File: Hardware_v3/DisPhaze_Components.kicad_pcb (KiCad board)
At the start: 2 copper layers, 60 x 110 mm, 83 parts, among them J1 SWD_Header, J2 Eurorack_16_pin_power, J3 PD1_Amt_In, J4 DAC1_Out, J5 PItch_In, J6 DAC2_Out, J7 PD2_Amt_In, J8 VCA_In, J9 USB_B_Micro, SW1 Octave_Switch, SW2 DAC1_RingMod_Switch, SW3 DAC2_Mix_Switch, SW4 SW_Push, U1 TL072, U2 MCP6004, U3 LM1117-3.3, U4 STM32F405RGTx, U5 LM4040DBZ-5, Y1 12MHz

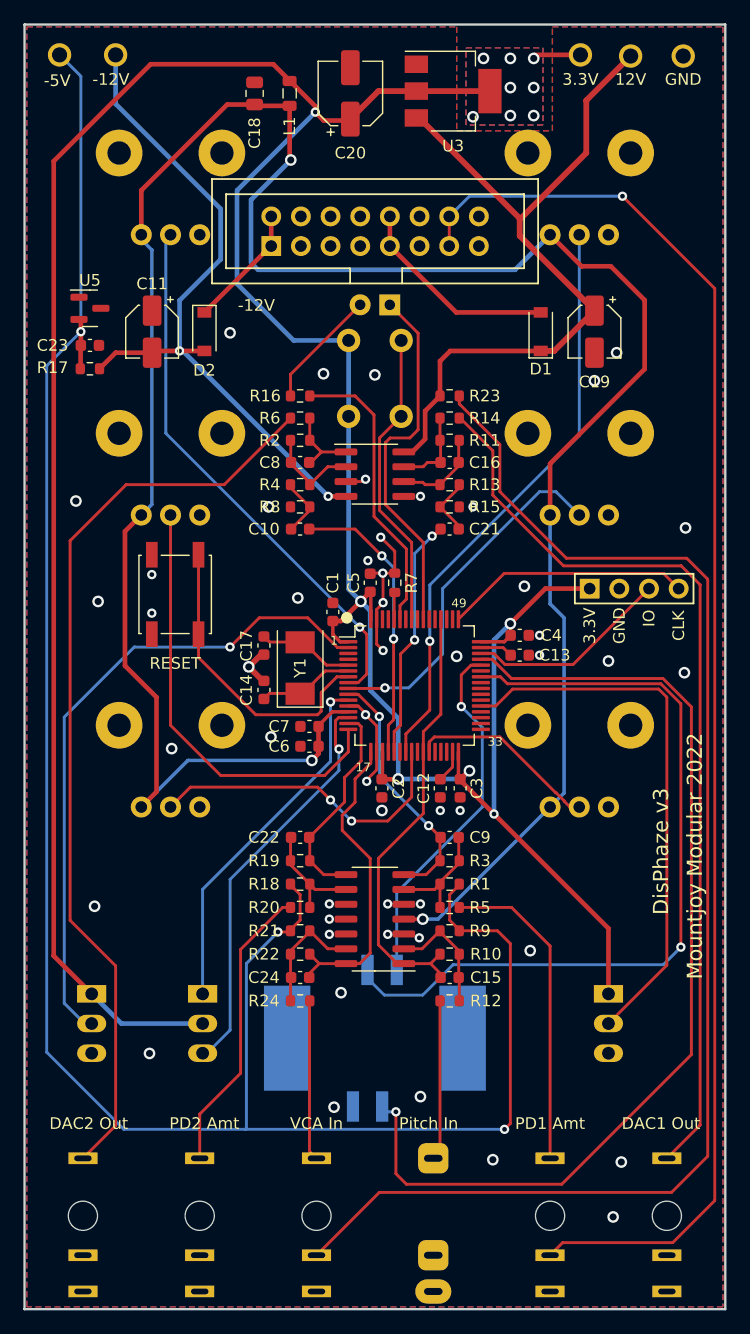
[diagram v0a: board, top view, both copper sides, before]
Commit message: Updated panel to incorporate v3 redesign
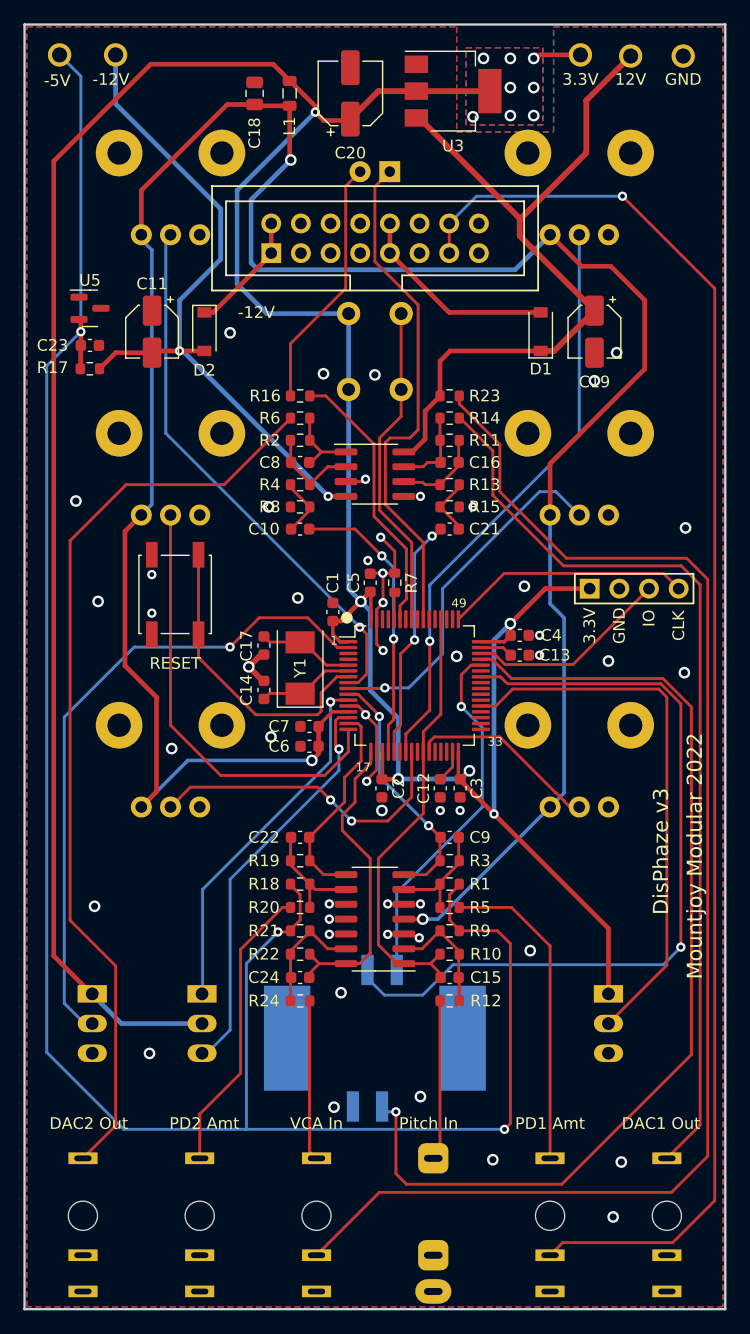
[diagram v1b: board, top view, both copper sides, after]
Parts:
- CTune1, FTune1, PD1Amt1, PD1Type1, PD2Amt1, PD2Type1: footprint Custom_Footprints:Alpha_9mm_Potentiometer -> Custom_Footprints:Alpha_9mm_Potentiometer_Aligned
- moved D3 11.4 mm to (131.3, 62.6)
- moved CTune1 7.91 mm to (147.5, 109.5), turned to 180 degrees
- moved FTune1 7.91 mm to (112.5, 109.5), turned to 180 degrees
- moved PD1Amt1 7.91 mm to (147.5, 60.5), turned to 180 degrees
- moved PD1Type1 7.91 mm to (147.5, 84.5), turned to 180 degrees
- moved PD2Amt1 7.91 mm to (112.5, 60.5), turned to 180 degrees
- moved PD2Type1 7.91 mm to (112.5, 84.5), turned to 180 degrees
- moved SW4 2.30 mm to (130.0, 78.0)
- moved J2 0.61 mm to (121.1, 69.6)
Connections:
- net /Action renamed /ACTION
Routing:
- net /LED_GREEN: track 31.4 -> 43.9 mm
- net Net-(D3-Pad2): track 10.3 -> 21.7 mm
- net /ACTION: track 25.8 -> 28.1 mm
- net /LED_RED: track 25.1 -> 23.6 mm

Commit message: Added photocoupler to MIDI Input
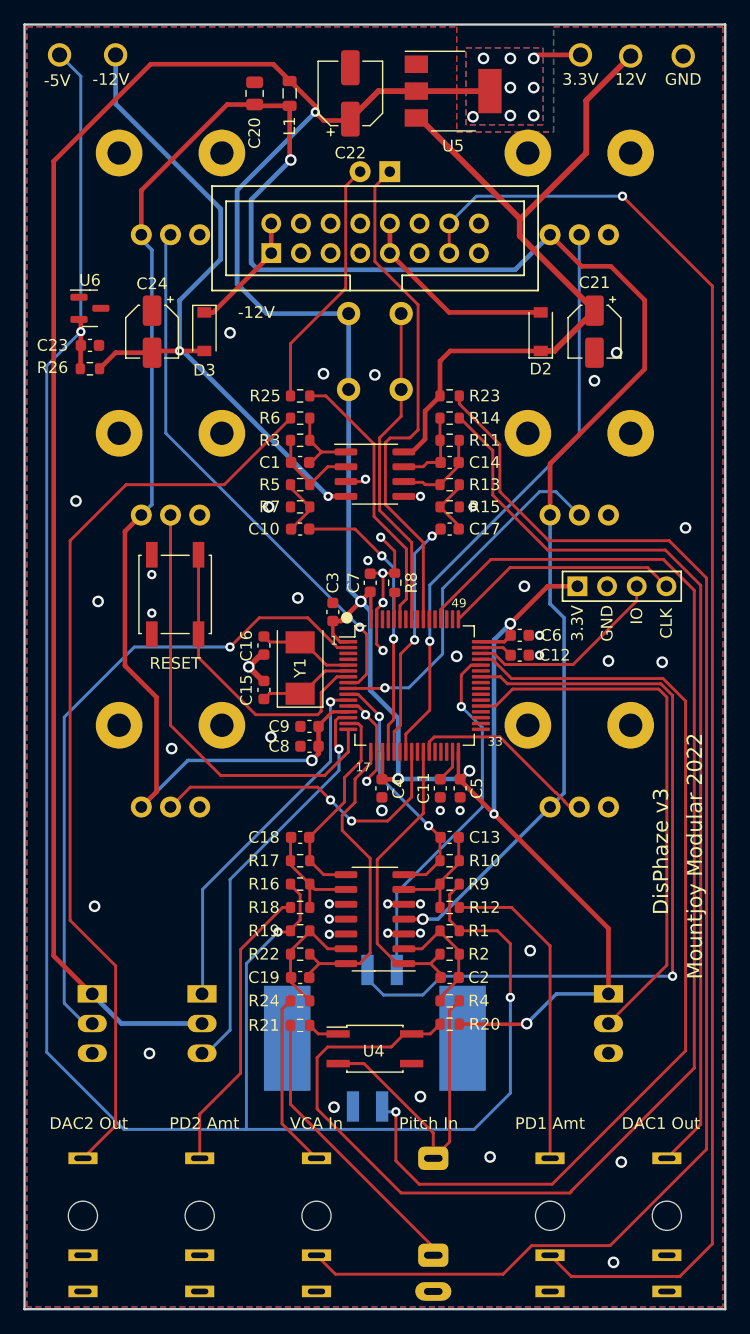
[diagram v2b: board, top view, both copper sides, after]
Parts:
- added R20: 10k, Resistor_SMD:R_0603_1608Metric, F.Cu at (136.4, 135.6)
- added R21: 220, Resistor_SMD:R_0603_1608Metric, F.Cu at (123.6, 135.7)
- added U4: LTV-356T, Package_SO:SO-4_4.4x3.6mm_P2.54mm, F.Cu at (130.0, 137.7)
- moved J6 1.07 mm to (147.3, 98.1)
- turned R24 to 180 degrees
- turned R4 to 0 degrees
- renumbered C8 to C1, C12 to C11, C13 to C12, C9 to C13, C16 to C14, C14 to C15, C17 to C16, C21 to C17, C22 to C18, C24 to C19, C15 to C2, C18 to C20, C19 to C21, C20 to C22, C11 to C24, C1 to C3, C2 to C4, C3 to C5, C4 to C6, C5 to C7, C6 to C8, C7 to C9, D3 to D1, D1 to D2, D2 to D3, J5 to J1, J4 to J2, J6 to J4, J7 to J5, J1 to J6, J9 to J7, J2 to J9, R9 to R1, R3 to R10, R5 to R12, R18 to R16, R19 to R17, R20 to R18, R21 to R19, R10 to R2, R16 to R25, R17 to R26, R2 to R3, R12 to R4, R4 to R5, R8 to R7, R7 to R8, R1 to R9, TP5 to TP1, TP1 to TP2, TP2 to TP3, TP3 to TP4, TP4 to TP5, U2 to U1, U1 to U2, U4 to U3, U3 to U5, U5 to U6
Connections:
- net /Pitch_In renamed /Pitch_MIDI_In
- C2 pad 2: /MIDI_RX -> /V_OCT_CV
- J1 pad R: unconnected-(J5-PadR) -> /MIDI_VREF
- R2 pad 1: /MIDI_RX -> /V_OCT_CV
- U1 pad 1: /MIDI_RX -> /V_OCT_CV
- U3 pad 26: /MIDI_RX -> /V_OCT_CV
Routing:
- net /MIDI_RX: track 37.9 -> 122.2 mm
- net /V_OCT_CV: track 0.00 -> 26.0 mm
- net /MIDI_VREF: track 0.00 -> 24.7 mm
- net /Pitch_MIDI_In: track 13.7 -> 29.4 mm
- net +3V3: track 277.1 -> 289.9 mm, vias 14 -> 15
- net /CV_IN: track 123.0 -> 126.4 mm
- net Net-(R21-Pad1): track 0.00 -> 2.73 mm
- net GND: track 26.4 -> 29.1 mm, vias 50 -> 49
- net /USB_DP: track 86.4 -> 84.9 mm
- net /AREF_-5: track 182.9 -> 181.4 mm
- net /VCA_In: track 13.7 -> 15.0 mm
- net Net-(J8-Pad2): track 117.0 -> 117.8 mm
- net /SWCLK: track 21.0 -> 20.3 mm
- net Net-(C2-Pad1): track 10.5 -> 11.2 mm
- net -12V: track 11.0 -> 10.3 mm
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
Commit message: Replaced optocoupler with transistor pair. Changed bi-colour LED to 3 lead device
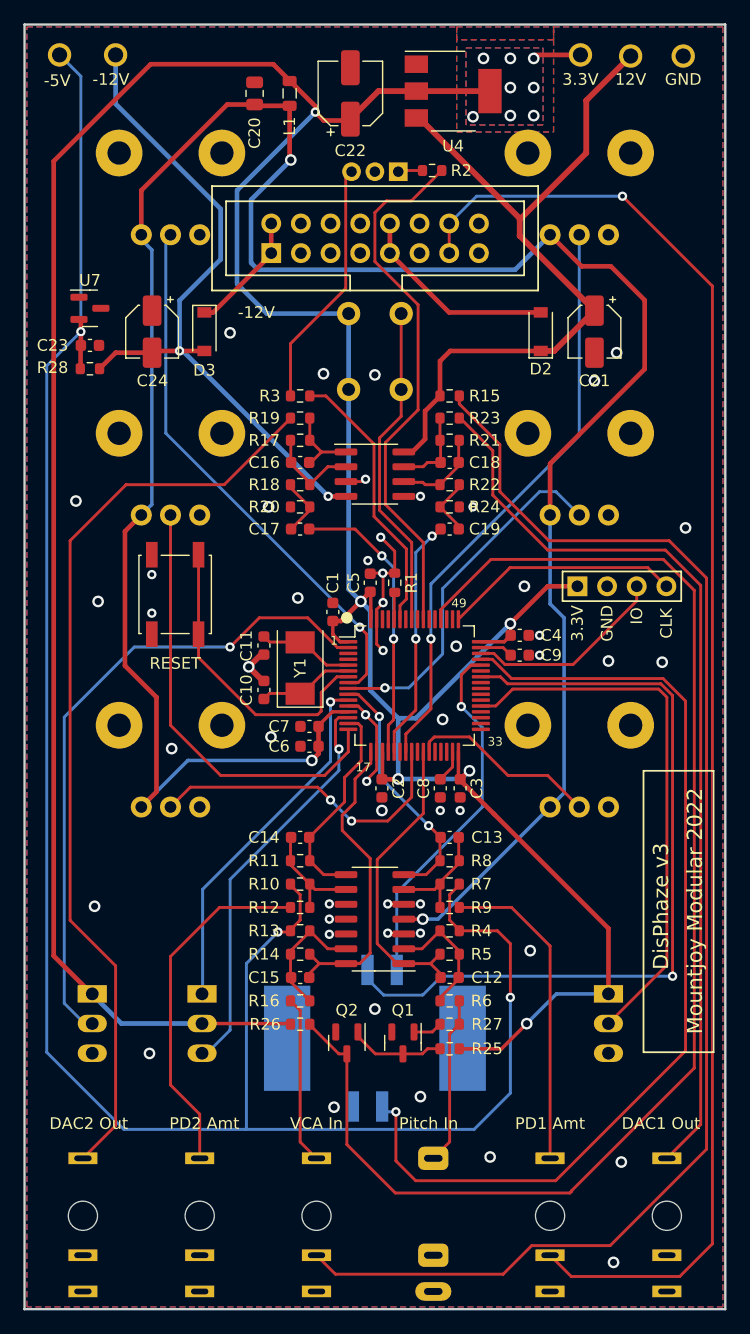
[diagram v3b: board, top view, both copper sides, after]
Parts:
- removed the R20 at (136.4, 135.6)
- removed the R21 at (123.6, 135.7)
- removed the U4 at (130.0, 137.7)
- added Q1: MMBT3904, Package_TO_SOT_SMD:SOT-23, F.Cu at (132.4, 137.2)
- added Q2: MMBT3904, Package_TO_SOT_SMD:SOT-23, F.Cu at (127.6, 137.2)
- added R25: 4k7, Resistor_SMD:R_0603_1608Metric, F.Cu at (136.4, 137.7)
- added R26: 4k7, Resistor_SMD:R_0603_1608Metric, F.Cu at (123.6, 135.6)
- added R27: 4k7, Resistor_SMD:R_0603_1608Metric, F.Cu at (136.4, 135.6)
- added R3: 1k, Resistor_SMD:R_0603_1608Metric, F.Cu at (123.6, 81.8)
- D1: value RG_LED -> LED_Dual_AKA; footprint LED_THT:LED_D3.0mm -> LED_THT:LED_D3.0mm-3
- moved R2 22.4 mm to (134.9, 62.5)
- moved D1 1.28 mm to (130.0, 62.6)
- renumbered C3 to C1, C15 to C10, C16 to C11, C2 to C12, C18 to C14, C19 to C15, C1 to C16, C10 to C17, C14 to C18, C17 to C19, C4 to C2, C5 to C3, C6 to C4, C7 to C5, C8 to C6, C9 to C7, C11 to C8, C12 to C9, J6 to J1, J7 to J2, J1 to J3, J3 to J4, J8 to J6, J2 to J7, J4 to J8, R8 to R1, R16 to R10, R17 to R11, R18 to R12, R19 to R13, R22 to R14, R23 to R15, R24 to R16, R3 to R17, R5 to R18, R6 to R19, R25 to R2, R7 to R20, R11 to R21, R13 to R22, R14 to R23, R15 to R24, R26 to R28, R1 to R4, R2 to R5, R4 to R6, R9 to R7, R10 to R8, R12 to R9, U3 to U1, U1 to U3, U5 to U4, U6 to U7
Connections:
- D1 pad 1: /LED_GREEN -> Net-(D1-Pad1)
- D1 pad 2: Net-(D1-Pad2) -> GND
- J3 pad R: /MIDI_VREF -> unconnected-(J3-PadR)
- R2 pad 1: Net-(D1-Pad2) -> Net-(D1-Pad1)
- U1 pad 55: /LED_GREEN -> /LED_RED
- U1 pad 59: /LED_RED -> /LED_GREEN
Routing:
- net /MIDI_VREF: track 24.7 -> 0.00 mm
- net /LED_RED: track 23.6 -> 46.1 mm
- net Net-(D1-Pad2): track 21.7 -> 0.00 mm
- net Net-(D1-Pad3): track 0.00 -> 21.4 mm
- net /LED_GREEN: track 43.9 -> 23.6 mm
- net /Pitch_MIDI_In: track 29.4 -> 14.4 mm
- net Net-(Q1-Pad3): track 0.00 -> 8.21 mm
- net /MIDI_RX: track 122.2 -> 114.3 mm
- net /PD2Amt_in: track 25.1 -> 30.3 mm
- net +3V3: track 289.9 -> 294.5 mm, vias 15 -> 14
- net Net-(R21-Pad1): track 2.73 -> 0.00 mm
- net Net-(Q1-Pad1): track 0.00 -> 2.60 mm
- net Net-(D1-Pad1): track 0.00 -> 2.12 mm
- net /VCA_In: track 15.0 -> 14.4 mm
- net GND: vias 49 -> 51

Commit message: Preparation of Gerbers for v3 hardware ordering
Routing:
- net VCC: track 65.3 -> 63.5 mm
- net /DAC1_RING_MOD: track 46.8 -> 46.2 mm
- net GND: vias 51 -> 53

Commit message: Started implementing v3 Polyphonic changes
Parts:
- C10, C11: value 18pF -> 30pF
- C16, C18: value 18pF -> 22pF
- Y1: value 12MHz -> 12MHz_18pF
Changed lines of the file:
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@@
       (effects (font (size 1 1) (thickness 0.15)))
     )
-    (fp_text value "18pF" (at 0 1.43 90) (layer "F.Fab")
+    (fp_text value "30pF" (at 0 1.43 90) (layer "F.Fab")
       (effects (font (size 1 1) (thickness 0.15)))
     )
@@
       (effects (font (size 1 1) (thickness 0.15)))
     )
-    (fp_text value "18pF" (at 0 1.43 90) (layer "F.Fab")
+    (fp_text value "30pF" (at 0 1.43 90) (layer "F.Fab")
       (effects (font (size 1 1) (thickness 0.15)))
     )
@@
       (effects (font (size 1 1) (thickness 0.15)))
     )
-    (fp_text value "18pF" (at 0 1.43) (layer "F.Fab")
+    (fp_text value "22pF" (at 0 1.43) (layer "F.Fab")
       (effects (font (size 1 1) (thickness 0.15)))
     )
@@
       (effects (font (size 1 1) (thickness 0.15)))
     )
-    (fp_text value "18pF" (at 0 1.43) (layer "F.Fab")
+    (fp_text value "22pF" (at 0 1.43) (layer "F.Fab")
       (effects (font (size 1 1) (thickness 0.15)))
     )
@@
       (effects (font (size 1 1) (thickness 0.15)))
     )
-    (fp_text value "12MHz" (at 0 2.95 90) (layer "F.Fab")
-      (effects (font (size 1 1) (thickness 0.15)))
-    )
+    (fp_text value "12MHz_18pF" (at 0 2.95 90) (layer "F.Fab")
+      (effects (font (size 1 1) (thickness 0.15)))
+    )

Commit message: More handling for MIDI issues
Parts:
- C16: value 22pF -> 1nF
- C18: value 22pF -> 1nf
- R17, R21: value 68k -> 10k
- R18, R22: value 6.8k -> 2k
- R4: value 91k -> 82k
- R5: value 56k -> 47k
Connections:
- J4 pad 2: /CV_IN -> GND
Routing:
- net /CV_IN: track 126.4 -> 0.00 mm, vias 1 -> 0
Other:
- board text added: "DisPhaze v3.1"
- board text removed: "DisPhaze v3"

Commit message: Fixed pd1 not responding in mono mode
Split original v3 schematics
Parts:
- C16: value 1nF -> 22pF
- C18: value 1nf -> 22pF
- R17, R21: value 10k -> 68k
- R18, R22: value 2k -> 6.8k
- R4: value 82k -> 91k
- R5: value 47k -> 56k
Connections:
- J4 pad 2: GND -> /CV_IN
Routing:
- net /CV_IN: track 0.00 -> 126.4 mm, vias 0 -> 1
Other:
- board text added: "DisPhaze v3"
- board text removed: "DisPhaze v3.1"
